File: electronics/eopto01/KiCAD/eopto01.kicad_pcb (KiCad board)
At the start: 2 copper layers, 33.5 x 8 mm, 21 parts, among them K1 CONN_3, Q1 BC849

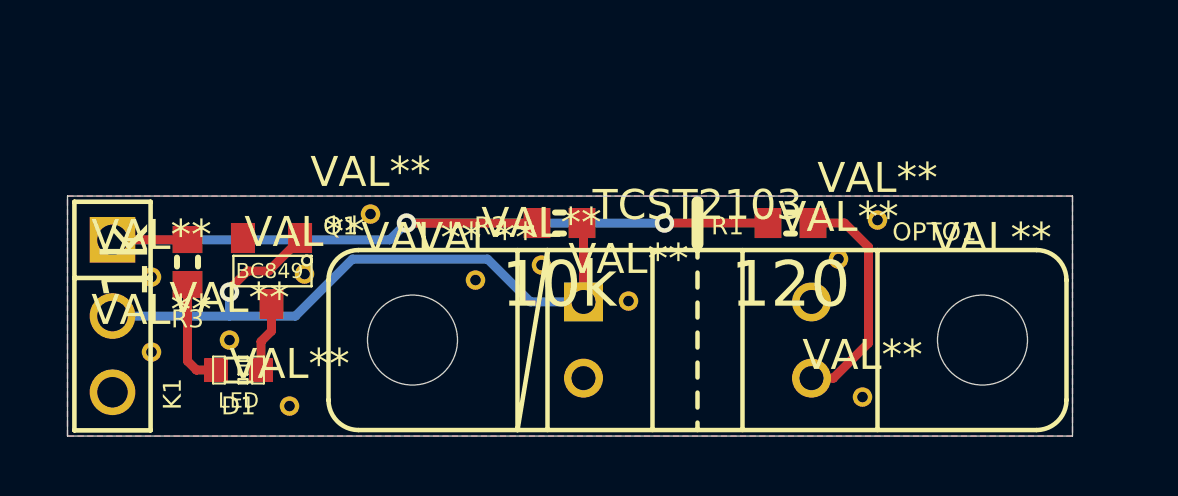
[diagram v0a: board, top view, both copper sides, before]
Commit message: Added JST connector for Opto-endstop
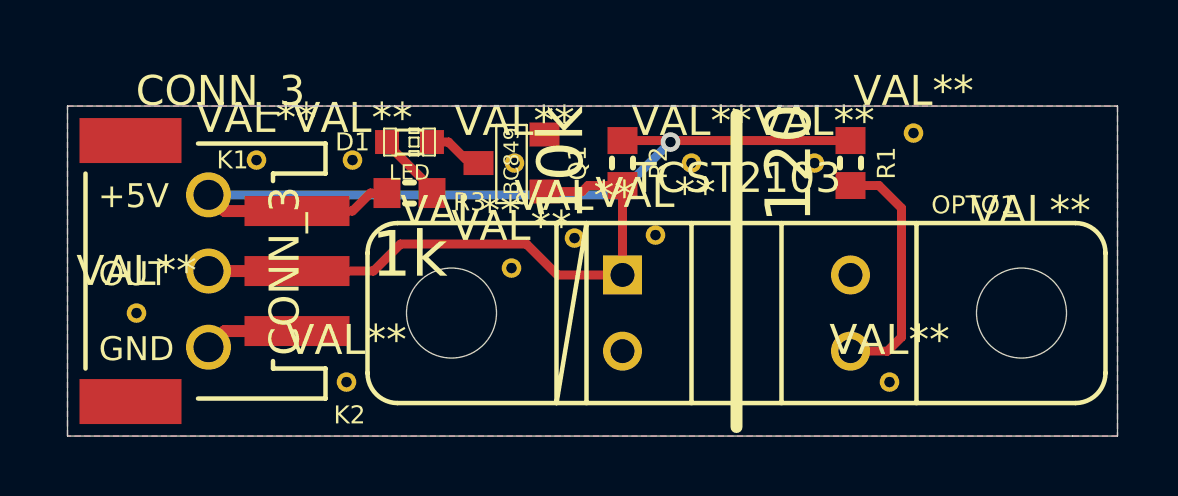
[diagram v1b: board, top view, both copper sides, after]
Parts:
- removed the ? at (194.4, 169.6)
- removed the ? at (183.1, 173.1)
- removed the ? at (178.5, 171.3)
- removed the ? at (178.5, 168.8)
- removed the ? at (185.8, 166.7)
- removed the ? at (181.1, 170.9)
- removed the ? at (183.6, 168.7)
- removed the ? at (189.3, 168.9)
- removed the ? at (191.5, 168.4)
- removed the ? at (201.4, 168.2)
- removed the ? at (202.7, 166.9)
- removed the ? at (202.2, 172.8)
- added ?: VAL**, Lerche_via_0.35mm_GND_MaskOver, F.Cu at (185.0, 172.3)
- added ?: VAL**, Lerche_via_0.35mm_GND_MaskOver, F.Cu at (178.0, 170.0)
- added ?: VAL**, Lerche_via_0.35mm_GND_MaskOver, F.Cu at (196.5, 165.0)
- added ?: VAL**, Lerche_via_0.35mm_GND_MaskOver, F.Cu at (195.3, 167.4)
- added ?: VAL**, Lerche_via_0.35mm_GND_MaskOver, F.Cu at (203.9, 164.0)
- added ?: VAL**, Lerche_via_0.35mm_GND_MaskOver, F.Cu at (182.0, 164.9)
- added ?: VAL**, Lerche_via_0.35mm_GND_MaskOver, F.Cu at (185.2, 164.9)
- added ?: VAL**, Lerche_via_0.35mm_GND_MaskOver, F.Cu at (190.6, 165.0)
- added ?: VAL**, Lerche_via_0.35mm_GND_MaskOver, F.Cu at (192.6, 167.5)
- added ?: VAL**, Lerche_via_0.35mm_GND_MaskOver, F.Cu at (200.6, 165.0)
- added ?: VAL**, Lerche_via_0.35mm_GND_MaskOver, F.Cu at (203.1, 172.3)
- added ?: VAL**, Lerche_via_0.35mm_GND_MaskOver, F.Cu at (190.5, 168.5)
- added K2: CONN_3, Lerche_JST_3P, F.Cu at (177.8, 168.6)
- K1: footprint PIN_ARRAY_3X1 -> Lerche_3P_2.54mm
- moved D1 9.50 mm to (187.1, 164.3)
- moved Q1 8.77 mm to (190.5, 165.0), turned to 90 degrees
- moved R3 7.75 mm to (187.1, 166.0), turned to 180 degrees
- moved K1 3.53 mm to (180.4, 168.6)
- moved R2 2.90 mm to (194.2, 165.0), turned to 90 degrees
- moved R1 2.83 mm to (201.8, 165.0), turned to 90 degrees
- moved ? 1.58 mm to (188.5, 170.0)
- moved ? 1.58 mm to (207.5, 170.0)
- moved OPTO1 1.58 mm to (198.0, 170.0)
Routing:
- net OPTO_OUT: track 23.7 -> 20.3 mm, vias 1 -> 0
- net GND: track 0.00 -> 3.17 mm
- net N-000002: track 3.63 -> 2.32 mm
- net +5V: track 28.9 -> 30.2 mm, vias 2 -> 1
- net N-000003: track 2.35 -> 1.84 mm
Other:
- board size 33.5 x 8 mm -> 35 x 11 mm

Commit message: Changed to MOSFET for LED
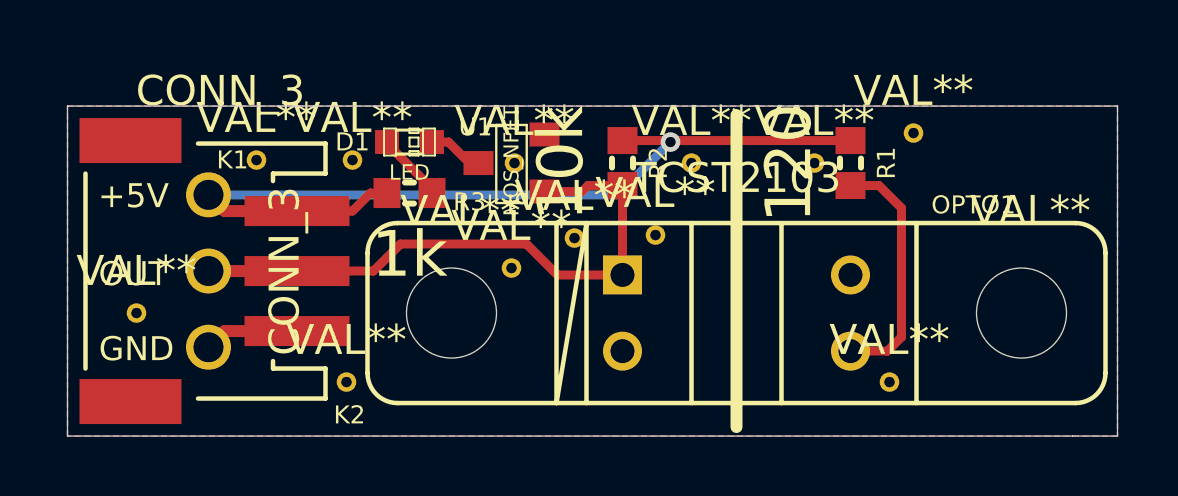
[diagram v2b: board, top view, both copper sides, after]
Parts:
- removed Q1: BC849, SOT23
- added U1: MOS_NFET, SOT23, F.Cu at (190.5, 165.0)
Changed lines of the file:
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@@
   )
   (setup
-    (last_trace_width 0.3)
+    (last_trace_width 0.16)
     (user_trace_width 0.16)
     (user_trace_width 0.2)
@@
   (net 1 +5V)
   (net 2 GND)
-  (net 3 N-000002)
-  (net 4 N-000003)
+  (net 3 N-000001)
+  (net 4 N-000002)
   (net 5 N-000005)
   (net 6 OPTO_OUT)
@@
     (add_net +5V)
     (add_net GND)
+    (add_net N-000001)
     (add_net N-000002)
-    (add_net N-000003)
     (add_net N-000005)
     (add_net OPTO_OUT)
@@
     (pad 1 smd rect (at -0.7493 0 90) (size 1 0.9)
       (layers F.Cu F.Paste F.Mask)
-      (net 3 N-000002)
+      (net 3 N-000001)
     )
     (pad 2 smd rect (at 0.7493 0 90) (size 1 0.9)
@@
     (pad 1 smd rect (at -0.7493 0) (size 0.79756 0.79756)
       (layers F.Cu F.Paste F.Mask)
-      (net 3 N-000002)
+      (net 3 N-000001)
     )
     (pad 2 smd rect (at 0.7493 0) (size 0.79756 0.79756)
       (layers F.Cu F.Paste F.Mask)
-      (net 4 N-000003)
-    )
-  )
-  (module SOT23 (layer F.Cu)
-    (at 190.5 165 90)
-    (tags SOT23)
-    (fp_text reference Q1 (at 0 2.2 90) (layer F.SilkS)
-      (effects (font (size 0.6 0.6) (thickness 0.1)))
-    )
-    (fp_text value BC849 (at 0.0635 0 90) (layer F.SilkS)
-      (effects (font (size 0.50038 0.50038) (thickness 0.09906)))
-    )
-    (fp_circle (center -1.17602 0.35052) (end -1.30048 0.44958) (layer F.SilkS) (width 0.07874))
-    (fp_line (start 1.27 -0.508) (end 1.27 0.508) (layer F.SilkS) (width 0.07874))
-    (fp_line (start -1.3335 -0.508) (end -1.3335 0.508) (layer F.SilkS) (width 0.07874))
-    (fp_line (start 1.27 0.508) (end -1.3335 0.508) (layer F.SilkS) (width 0.07874))
-    (fp_line (start -1.3335 -0.508) (end 1.27 -0.508) (layer F.SilkS) (width 0.07874))
-    (pad 3 smd rect (at 0 -1.09982 90) (size 0.8001 1.00076)
-      (layers F.Cu F.Paste F.Mask)
-      (net 4 N-000003)
-    )
-    (pad 2 smd rect (at 0.9525 1.09982 90) (size 0.8001 1.00076)
-      (layers F.Cu F.Paste F.Mask)
-      (net 2 GND)
-    )
-    (pad 1 smd rect (at -0.9525 1.09982 90) (size 0.8001 1.00076)
-      (layers F.Cu F.Paste F.Mask)
-      (net 6 OPTO_OUT)
-    )
-    (model smd\SOT23_3.wrl
-      (at (xyz 0 0 0))
-      (scale (xyz 0.4 0.4 0.4))
-      (rotate (xyz 0 0 180))
+      (net 4 N-000002)
     )
   )
@@
       (clearance 0.001)
       (zone_connect 2)
+    )
+  )
+  (module SOT23 (layer F.Cu)
+    (at 190.5 165 90)
+    (tags SOT23)
+    (fp_text reference U1 (at 1.2 -1.2 180) (layer F.SilkS)
+      (effects (font (size 0.6 0.6) (thickness 0.1)))
+    )
+    (fp_text value MOS_NFET (at 0.0635 0 90) (layer F.SilkS)
+      (effects (font (size 0.50038 0.50038) (thickness 0.09906)))
+    )
+    (fp_circle (center -1.17602 0.35052) (end -1.30048 0.44958) (layer F.SilkS) (width 0.07874))
+    (fp_line (start 1.27 -0.508) (end 1.27 0.508) (layer F.SilkS) (width 0.07874))
+    (fp_line (start -1.3335 -0.508) (end -1.3335 0.508) (layer F.SilkS) (width 0.07874))
+    (fp_line (start 1.27 0.508) (end -1.3335 0.508) (layer F.SilkS) (width 0.07874))
+    (fp_line (start -1.3335 -0.508) (end 1.27 -0.508) (layer F.SilkS) (width 0.07874))
+    (pad 3 smd rect (at 0 -1.09982 90) (size 0.8001 1.00076)
+      (layers F.Cu F.Paste F.Mask)
+      (net 4 N-000002)
+    )
+    (pad 2 smd rect (at 0.9525 1.09982 90) (size 0.8001 1.00076)
+      (layers F.Cu F.Paste F.Mask)
+      (net 2 GND)
+    )
+    (pad 1 smd rect (at -0.9525 1.09982 90) (size 0.8001 1.00076)
+      (layers F.Cu F.Paste F.Mask)
+      (net 6 OPTO_OUT)
+    )
+    (model smd\SOT23_3.wrl
+      (at (xyz 0 0 0))
+      (scale (xyz 0.4 0.4 0.4))
+      (rotate (xyz 0 0 180))
     )
   )
@@
   (segment (start 187.8493 165.8493) (end 187.8493 166) (width 0.3) (layer F.Cu) (net 3))
   (segment (start 186.3507 164.3507) (end 187.8493 165.8493) (width 0.3) (layer F.Cu) (net 3))
+  (segment (start 188.4 164.3) (end 187.8493 164.3) (width 0.3) (layer F.Cu) (net 4))
   (segment (start 189.40018 165) (end 189.1 165) (width 0.3) (layer F.Cu) (net 4))
-  (segment (start 188.4 164.3) (end 187.8493 164.3) (width 0.3) (layer F.Cu) (net 4))
   (segment (start 189.1 165) (end 188.4 164.3) (width 0.3) (layer F.Cu) (net 4))
   (segment (start 201.8 165.7493) (end 202.7493 165.7493) (width 0.3) (layer F.Cu) (net 5))
